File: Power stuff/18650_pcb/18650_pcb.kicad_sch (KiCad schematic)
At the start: 44 parts, among them J1 Conn_01x20, J2 CONN_01X02, J3 Conn_01x01, J4 Conn_01x01, J5 Conn_01x01, J6 Conn_01x02_MountingPin, Q1 LL P-FET, Q2 IRLML6401, Q3 Q_NPN_BCE, Q4 LL P-FET, Q5 Q_NPN_BCE, SW1 BUTTON, U1 TP4056_BREAKOUT, U2 DC_DC_BREAKOUT, U4 AP2112K-3.3, U5 AP1117-33

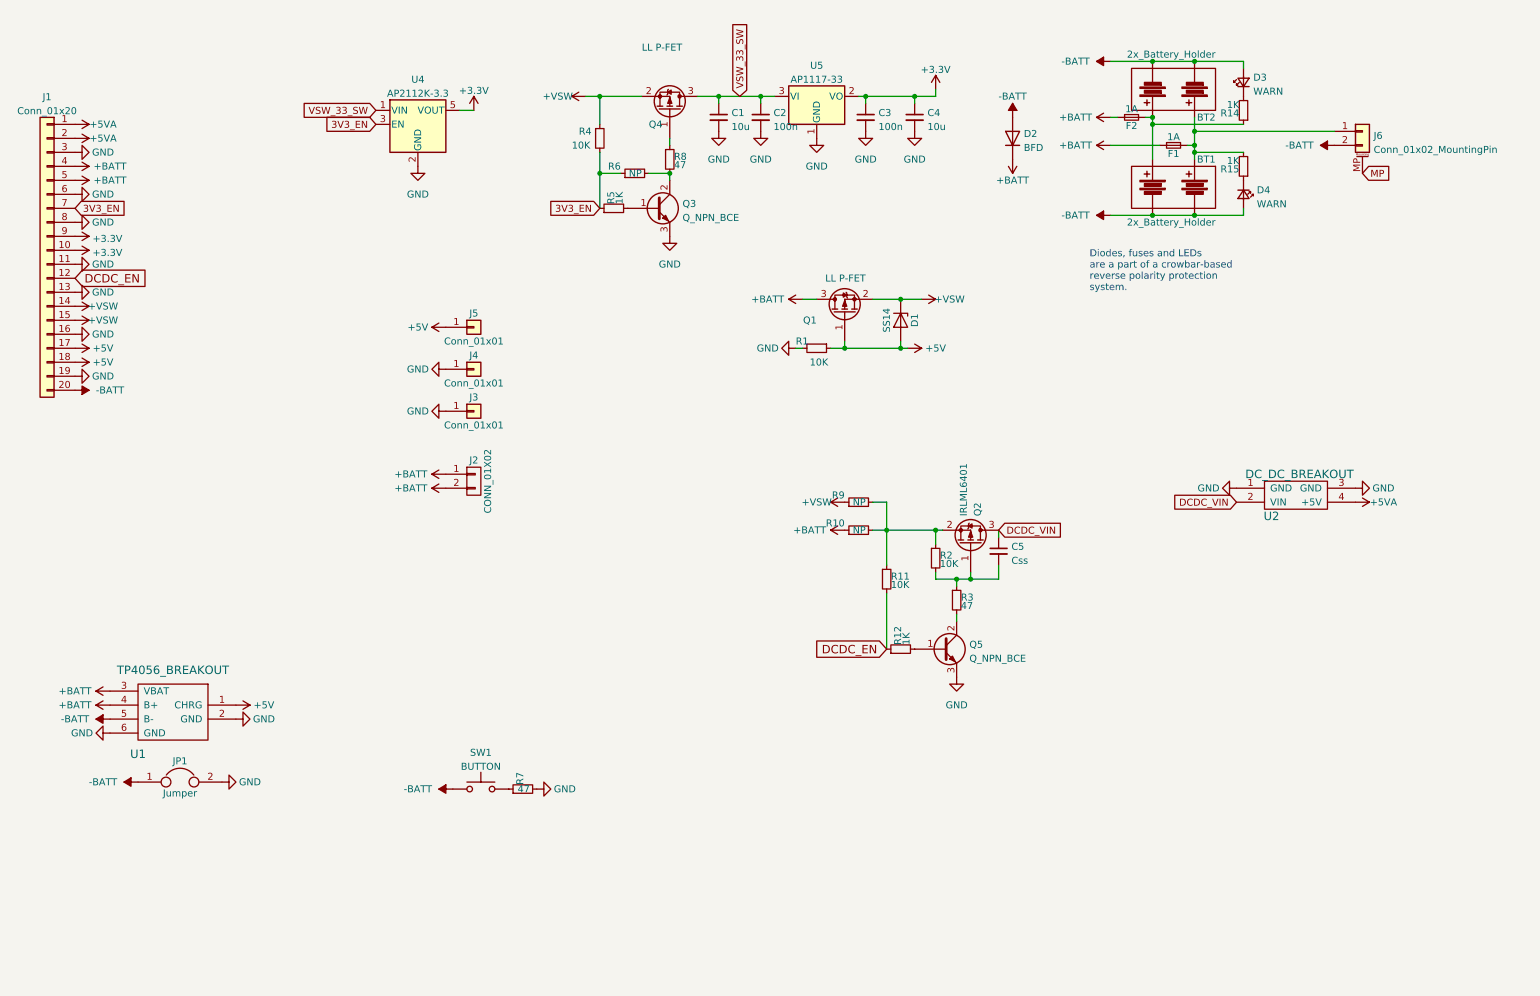
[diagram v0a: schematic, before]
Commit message: 18650_pcb: WIP v3, added USB-C socket for charging, need to fix silk
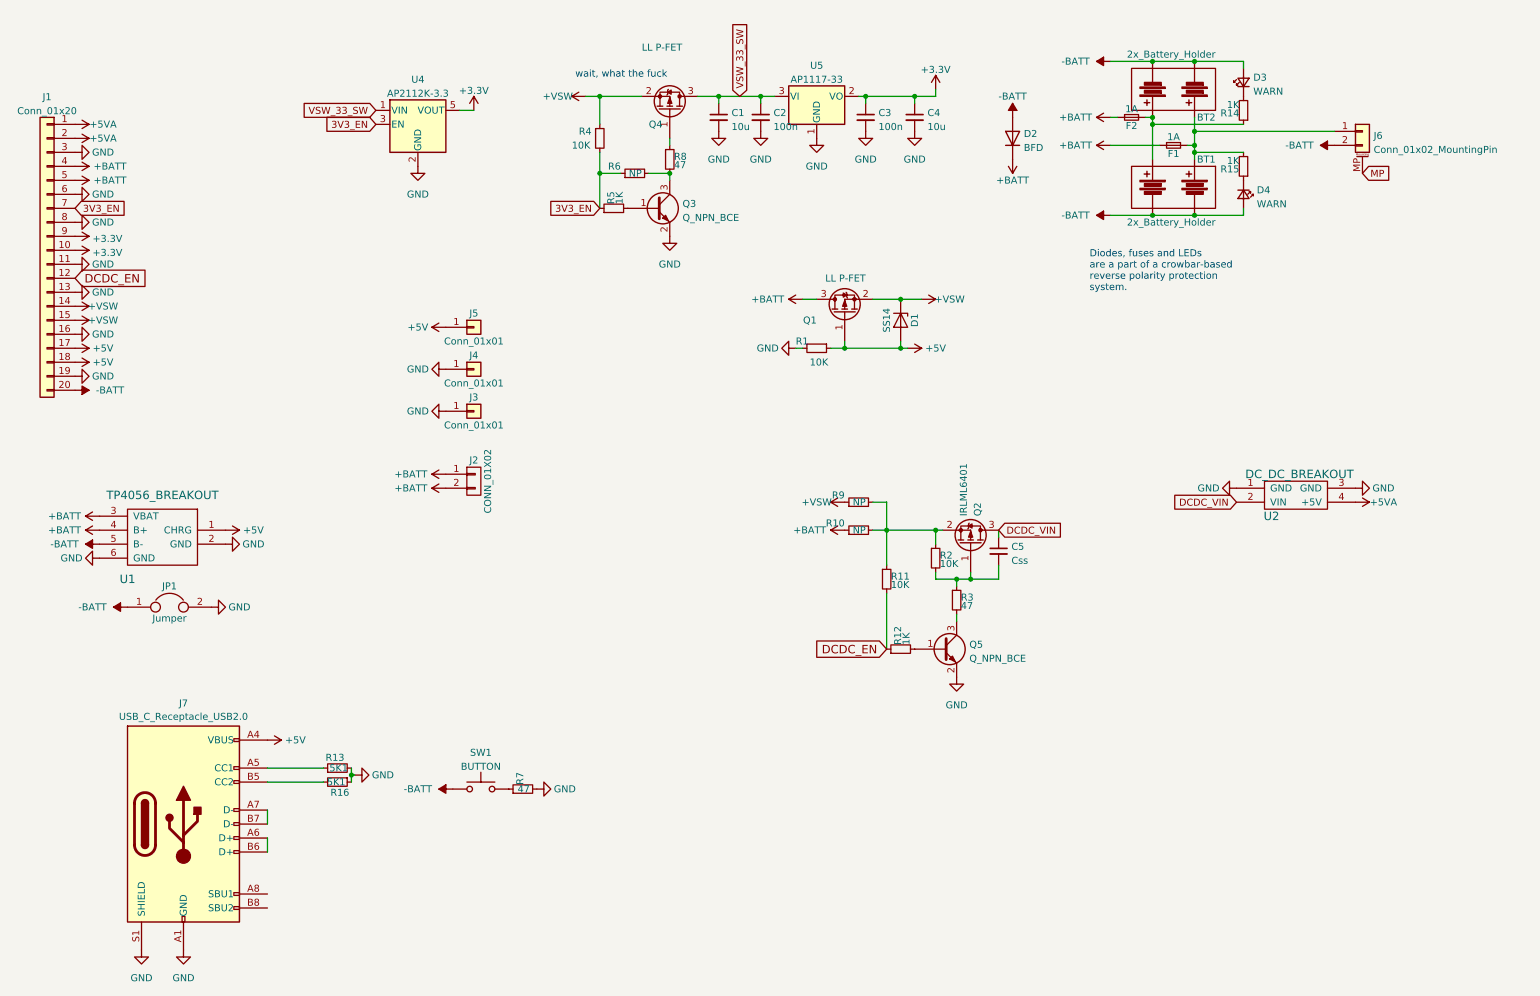
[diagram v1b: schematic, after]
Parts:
- added J7: USB_C_Receptacle_USB2.0, Connector_USB:USB_C_Receptacle_HRO_TYPE-C-31-M-12, symbol Connector:USB_C_Receptacle_USB2.0
- added R13, R16: 5K1, Resistor_SMD:R_0805_2012Metric, symbol 18650_pcb-rescue:R_Small
- Q3, Q5: symbol Device:Q_NPN_BCE -> Device:Q_NPN_BEC
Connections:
- net +5V: now also J7.A4 (VBUS), J7.A9 (VBUS), J7.B4 (VBUS), J7.B9 (VBUS)
- net GND: now also Q3.2 (E), Q5.2 (E), J7.A1 (GND), J7.A12 (GND), J7.B1 (GND), J7.B12 (GND), J7.S1 (SHIELD), R13.2, R16.1; no longer Q3.3 (E), Q5.3 (E)
- net at R3.2: now also Q5.3 (C); no longer Q5.2 (C)
- net at R6.2, R8.2: now also Q3.3 (C); no longer Q3.2 (C)
- new net: J7.A5 (CC1), R13.1
- new net: J7.A6 (D+), J7.B6 (D+)
- new net: J7.A7 (D-), J7.B7 (D-)
- new net: J7.B5 (CC2), R16.2
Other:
- note added: "wait, what the fuck"
- moved on the sheet: JP1, U1

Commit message: 18650_pcb: proper v3, added usb-c socket usb data breakout, mounting holes on corners, improved silk including LED warnings, rerouted LEDs for short-circuit protection with 18650 hoplder pads
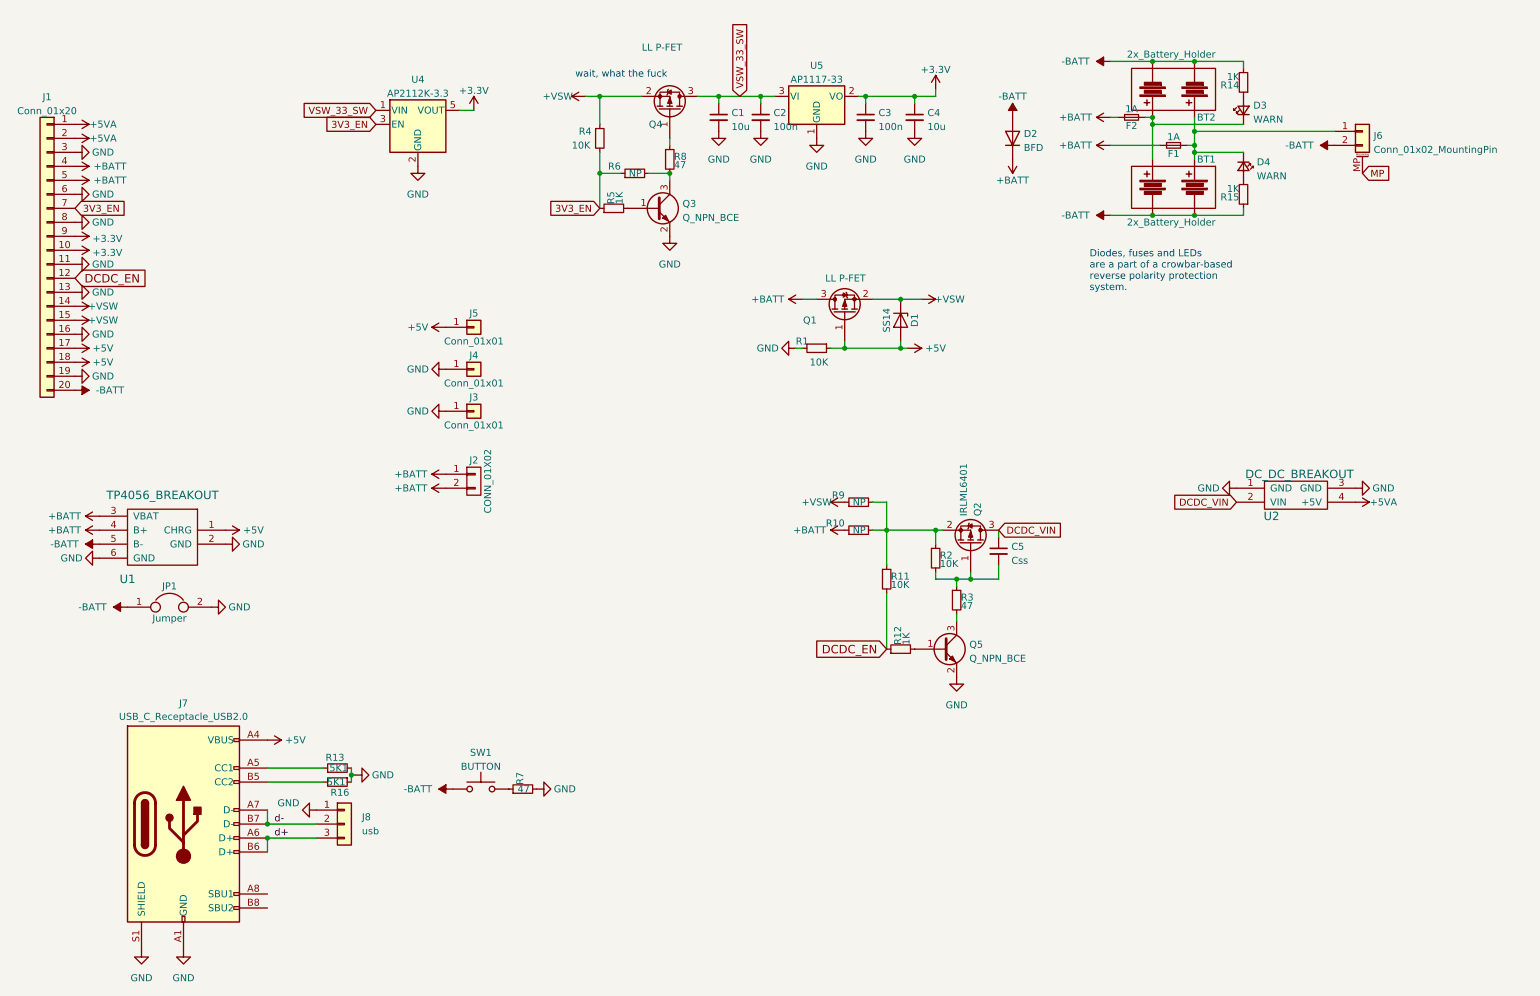
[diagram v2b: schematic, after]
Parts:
- added J8: usb, Connector_PinHeader_2.54mm:PinHeader_1x03_P2.54mm_Vertical, symbol Connector_Generic:Conn_01x03
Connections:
- net -BATT: now also R14.2, R15.1; no longer D3.2 (A), D4.2 (A)
- net GND: now also J8.1 (Pin_1)
- net at BT1.1, BT2.1, F1.2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: now also D4.1 (K); no longer R15.2
- net at BT1.2, BT2.2, F2.2: now also D3.1 (K); no longer R14.1
- net d+: now reaches J7.A6 (D+), J7.B6 (D+)
- net d+: now also J8.3 (Pin_3)
- net d-: now reaches J7.A7 (D-), J7.B7 (D-)
- net d-: now also J8.2 (Pin_2)
- new net: D3.2 (A), R14.1
- new net: D4.2 (A), R15.2
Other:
- moved on the sheet: D3, D4, R14, R15
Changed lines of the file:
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@@
   (junction (at 182.88 109.22) (diameter 0) (color 0 0 0 0)
   )
+  (junction (at 61.595 165.1) (diameter 0) (color 0 0 0 0)
+  )
   (junction (at 166.37 76.2) (diameter 0) (color 0 0 0 0)
   )
   (junction (at 222.25 34.29) (diameter 0) (color 0 0 0 0)
   )
+  (junction (at 61.595 162.56) (diameter 0) (color 0 0 0 0)
+  )
   (junction (at 229.87 36.83) (diameter 0) (color 0 0 0 0)
   )
@@
     (stroke (width 0) (type default))
   )
+  (wire (pts (xy 61.595 160.02) (xy 61.595 162.56))
+    (stroke (width 0) (type default))
+  )
   (wire (pts (xy 186.69 125.73) (xy 186.69 124.46))
     (stroke (width 0) (type default))
@@
     (stroke (width 0) (type default))
   )
+  (wire (pts (xy 70.485 162.56) (xy 61.595 162.56))
+    (stroke (width 0) (type default))
+  )
   (wire (pts (xy 214.63 39.37) (xy 223.52 39.37))
     (stroke (width 0) (type default))
@@
     (stroke (width 0) (type default))
   )
+  (wire (pts (xy 70.485 165.1) (xy 61.595 165.1))
+    (stroke (width 0) (type default))
+  )
   (wire (pts (xy 214.63 34.29) (xy 215.9 34.29))
     (stroke (width 0) (type default))
@@
   )
   (wire (pts (xy 182.88 116.84) (xy 182.88 118.11))
-    (stroke (width 0) (type default))
-  )
-  (wire (pts (xy 61.595 160.02) (xy 61.595 162.56))
     (stroke (width 0) (type default))
   )
@@
   (text "Diodes, fuses and LEDs\nare a part of a crowbar-based\nreverse polarity protection\nsystem."
     (at 210.82 66.04 0)
+    (effects (font (size 1.27 1.27)) (justify left bottom))
+  )
+  (label "d-" (at 62.865 162.56 0) (fields_autoplaced)
+    (effects (font (size 1.27 1.27)) (justify left bottom))
+  )
+  (label "d+" (at 62.865 165.1 0) (fields_autoplaced)
     (effects (font (size 1.27 1.27)) (justify left bottom))
   )
@@
     )
   )
+  (symbol (lib_id "Connector_Generic:Conn_01x03") (at 75.565 162.56 0) (unit 1)
+    (in_bom yes) (on_board yes) (dnp no) (fields_autoplaced)
+    (property "Reference" "J8" (at 78.74 161.29 0)
+      (effects (font (size 1.27 1.27)) (justify left))
+    )
+    (property "Value" "usb" (at 78.74 163.83 0)
+      (effects (font (size 1.27 1.27)) (justify left))
+    )
+    (property "Footprint" "Connector_PinHeader_2.54mm:PinHeader_1x03_P2.54mm_Vertical" (at 75.565 162.56 0)
+      (effects (font (size 1.27 1.27)) hide)
+    )
+    (property "Datasheet" "~" (at 75.565 162.56 0)
+      (effects (font (size 1.27 1.27)) hide)
+    )
+    (pin "2")
+    (pin "1")
+    (pin "3")
+    (instances
+      (project "18650_pcb"
+        (path "/2ca39f1d-3cce-4c44-b7ca-63071900b67d"
+          (reference "J8") (unit 1)
+        )
+      )
+    )
+  )
   (symbol (lib_id "18650_pcb-rescue:+VSW") (at 26.67 71.12 270) (unit 1)
     (in_bom yes) (on_board yes) (dnp no)
@@
     )
   )
-  (symbol (lib_id "Device:LED_Small") (at 238.76 27.94 90) (unit 1)
+  (symbol (lib_id "Device:LED_Small") (at 238.76 33.02 90) (unit 1)
     (in_bom yes) (on_board yes) (dnp no) (fields_autoplaced)
-    (property "Reference" "D3" (at 240.538 27.0418 90)
+    (property "Reference" "D3" (at 240.538 32.1218 90)
       (effects (font (size 1.27 1.27)) (justify right))
     )
-    (property "Value" "WARN" (at 240.538 29.5787 90)
+    (property "Value" "WARN" (at 240.538 34.6587 90)
       (effects (font (size 1.27 1.27)) (justify right))
     )
-    (property "Footprint" "LED_SMD:LED_0805_2012Metric" (at 238.76 27.94 90)
-      (effects (font (size 1.27 1.27)) hide)
-    )
-    (property "Datasheet" "~" (at 238.76 27.94 90)
+    (property "Footprint" "LED_SMD:LED_0805_2012Metric" (at 238.76 33.02 90)
+      (effects (font (size 1.27 1.27)) hide)
+    )
+    (property "Datasheet" "~" (at 238.76 33.02 90)
       (effects (font (size 1.27 1.27)) hide)
     )
@@
         (path "/2ca39f1d-3cce-4c44-b7ca-63071900b67d"
           (reference "R6") (unit 1)
+        )
+      )
+    )
+  )
+  (symbol (lib_id "18650_pcb-rescue:GND") (at 70.485 160.02 270) (unit 1)
+    (in_bom yes) (on_board yes) (dnp no)
+    (property "Reference" "#PWR023" (at 64.135 160.02 0)
+      (effects (font (size 1.27 1.27)) hide)
+    )
+    (property "Value" "GND" (at 65.405 158.75 90)
+      (effects (font (size 1.27 1.27)))
+    )
+    (property "Footprint" "" (at 70.485 160.02 0)
+      (effects (font (size 1.27 1.27)) hide)
+    )
+    (property "Datasheet" "" (at 70.485 160.02 0)
+      (effects (font (size 1.27 1.27)) hide)
+    )
+    (pin "1")
+    (instances
+      (project "18650_pcb"
+        (path "/2ca39f1d-3cce-4c44-b7ca-63071900b67d"
+          (reference "#PWR023") (unit 1)
         )
       )
@@
     )
   )
-  (symbol (lib_id "Device:LED_Small") (at 238.76 48.26 270) (unit 1)
+  (symbol (lib_id "Device:LED_Small") (at 238.76 43.18 270) (unit 1)
     (in_bom yes) (on_board yes) (dnp no) (fields_autoplaced)
-    (property "Reference" "D4" (at 241.173 47.4888 90)
-      (effects (font (size 1.27 1.27)) (justify left))
-    )
-    (property "Value" "WARN" (at 241.173 50.0257 90)
-      (effects (font (size 1.27 1.27)) (justify left))
-    )
-    (property "Footprint" "LED_SMD:LED_0805_2012Metric" (at 238.76 48.26 90)
-      (effects (font (size 1.27 1.27)) hide)
-    )
-    (property "Datasheet" "~" (at 238.76 48.26 90)
+    (property "Reference" "D4" (at 241.173 42.4088 90)
+      (effects (font (size 1.27 1.27)) (justify left))
+    )
+    (property "Value" "WARN" (at 241.173 44.9457 90)
+      (effects (font (size 1.27 1.27)) (justify left))
+    )
+    (property "Footprint" "LED_SMD:LED_0805_2012Metric" (at 238.76 43.18 90)
+      (effects (font (size 1.27 1.27)) hide)
+    )
+    (property "Datasheet" "~" (at 238.76 43.18 90)
       (effects (font (size 1.27 1.27)) hide)
     )
@@
     )
   )
-  (symbol (lib_id "18650_pcb-rescue:R_Small") (at 238.76 43.18 180) (unit 1)
-    (in_bom yes) (on_board yes) (dnp no)
-    (property "Reference" "R15" (at 237.998 43.688 0)
-      (effects (font (size 1.27 1.27)) (justify left))
-    )
-    (property "Value" "1K" (at 237.998 42.164 0)
-      (effects (font (size 1.27 1.27)) (justify left))
-    )
-    (property "Footprint" "Resistor_SMD:R_0805_2012Metric" (at 238.76 43.18 0)
-      (effects (font (size 1.27 1.27)) hide)
-    )
-    (property "Datasheet" "" (at 238.76 43.18 0)
+  (symbol (lib_id "18650_pcb-rescue:R_Small") (at 238.76 48.26 180) (unit 1)
+    (in_bom yes) (on_board yes) (dnp no)
+    (property "Reference" "R15" (at 237.998 48.768 0)
+      (effects (font (size 1.27 1.27)) (justify left))
+    )
+    (property "Value" "1K" (at 237.998 47.244 0)
+      (effects (font (size 1.27 1.27)) (justify left))
+    )
+    (property "Footprint" "Resistor_SMD:R_0805_2012Metric" (at 238.76 48.26 0)
+      (effects (font (size 1.27 1.27)) hide)
+    )
+    (property "Datasheet" "" (at 238.76 48.26 0)
       (effects (font (size 1.27 1.27)) hide)
     )
@@
     )
   )
-  (symbol (lib_id "18650_pcb-rescue:R_Small") (at 238.76 33.02 180) (unit 1)
-    (in_bom yes) (on_board yes) (dnp no)
-    (property "Reference" "R14" (at 237.998 33.528 0)
-      (effects (font (size 1.27 1.27)) (justify left))
-    )
-    (property "Value" "1K" (at 237.998 32.004 0)
-      (effects (font (size 1.27 1.27)) (justify left))
-    )
-    (property "Footprint" "Resistor_SMD:R_0805_2012Metric" (at 238.76 33.02 0)
-      (effects (font (size 1.27 1.27)) hide)
-    )
-    (property "Datasheet" "" (at 238.76 33.02 0)
-      (effects (font (size 1.27 1.27)) hide)
-    )
+  (symbol (lib_id "18650_pcb-rescue:R_Small") (at 238.76 27.94 180) (unit 1)
+    (in_bom yes) (on_board yes) (dnp no)
+    (property "Reference" "R14" (at 237.998 28.448 0)
+      (effects (font (size 1.27 1.27)) (justify left))
+    )
+    (property "Value" "1K" (at 237.998 26.924 0)
+      (effects (font (size 1.27 1.27)) (justify left))
+    )
+    (property "Footprint" "Resistor_SMD:R_0805_2012Metric" (at 238.76 27.94 0)
+      (effects (font (size 1.27 1.27)) hide)
+    )
+    (property "Datasheet" "" (at 238.76 27.94 0)
+      (effects (font (size 1.27 1.27)) hide)
+    )
